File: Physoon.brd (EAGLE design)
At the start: 100 x 80 mm, 45 parts, among them IC2 74AHC1G125DBV, IC3 74AHC1G125DBV, M1 HX1, X1 BU-SMA-V

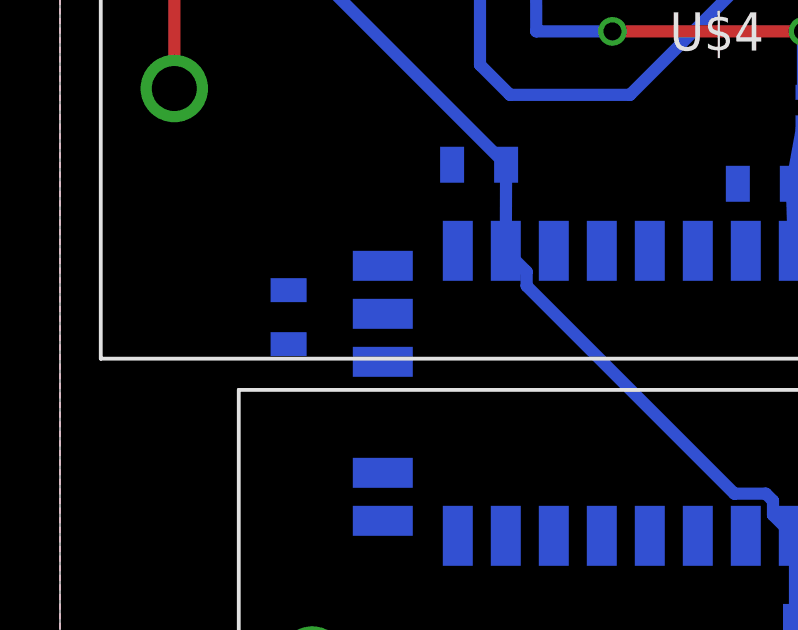
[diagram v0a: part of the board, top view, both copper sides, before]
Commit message: Fix GPS wiring
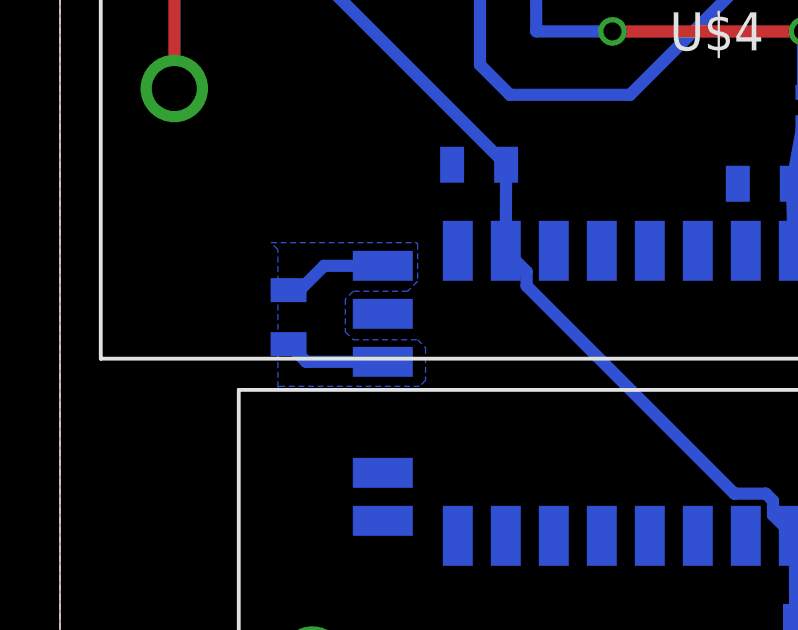
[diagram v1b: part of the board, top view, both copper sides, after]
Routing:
- net GND: track 16.6 -> 23.1 mm
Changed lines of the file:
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@@
 <setting verticaltext="up"/>
 </settings>
-<grid distance="1.3" unitdist="mil" unit="mil" style="lines" multiple="1" display="yes" altdistance="0.1" altunitdist="mm" altunit="mm"/>
+<grid distance="1.3" unitdist="mil" unit="inch" style="lines" multiple="1" display="yes" altdistance="0.00393700787" altunitdist="inch" altunit="inch"/>
 <layers>
 <layer number="1" name="Top" color="4" fill="1" visible="yes" active="yes"/>
@@
 <wire x1="29.21" y1="23.75" x2="29.26" y2="23.8" width="0.4064" layer="16"/>
 <wire x1="7.62" y1="20.69" x2="7.99" y2="20.69" width="0.4064" layer="16"/>
-<wire x1="10.65" y1="21.59" x2="10.76" y2="21.7" width="0.4064" layer="16"/>
-<wire x1="7.62" y1="22.49" x2="7.99" y2="22.49" width="0.4064" layer="16"/>
+<wire x1="10.76" y1="21.7" x2="10.65" y2="21.59" width="0.4064" layer="16"/>
+<wire x1="7.99" y1="22.49" x2="7.62" y2="22.49" width="0.4064" layer="16"/>
 <wire x1="63.285" y1="48.895" x2="63.5" y2="48.68" width="0.4064" layer="16"/>
 <wire x1="66.2186" y1="58.9386" x2="66.02" y2="58.74" width="0.4064" layer="16"/>
@@
 <wire x1="29.68496875" y1="50.132825" x2="29.2375625" y2="50.132825" width="0.4064" layer="16"/>
 <wire x1="29.2375625" y1="50.132825" x2="28.2833375" y2="49.1786" width="0.4064" layer="16"/>
+<wire x1="10.76" y1="23.3" x2="8.8" y2="23.3" width="0.4064" layer="16"/>
+<wire x1="8.8" y1="23.3" x2="7.99" y2="22.49" width="0.4064" layer="16"/>
+<wire x1="10.76" y1="20.1" x2="8.21" y2="20.1" width="0.4064" layer="16"/>
+<wire x1="8.21" y1="20.1" x2="7.62" y2="20.69" width="0.4064" layer="16"/>
+<wire x1="10.765859375" y1="21.694140625" x2="10.76" y2="21.7" width="0.4064" layer="16"/>
+<polygon width="0.000253125" layer="16" pour="cutout" isolate="0.3048">
+<vertex x="7.033259375" y="24.07158125"/>
+<vertex x="11.887196875" y="24.07158125"/>
+<vertex x="11.92021875" y="24.038559375"/>
+<vertex x="11.92021875" y="22.7838"/>
+<vertex x="11.59001875" y="22.4536"/>
+<vertex x="9.77391875" y="22.4536"/>
+<vertex x="9.509759375" y="22.189440625"/>
+<vertex x="9.509759375" y="21.099778125"/>
+<vertex x="9.77391875" y="20.83561875"/>
+<vertex x="11.920221875" y="20.83561875"/>
+<vertex x="12.18438125" y="20.571459375"/>
+<vertex x="12.18438125" y="19.481803125"/>
+<vertex x="11.986259375" y="19.28368125"/>
+<vertex x="7.297421875" y="19.28368125"/>
+<vertex x="7.2644" y="19.250659375"/>
+<vertex x="7.2644" y="23.840440625"/>
+</polygon>
 </signal>
 <signal name="PDI-DATA">
